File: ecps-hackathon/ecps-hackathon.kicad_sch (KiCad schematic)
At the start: 4 parts, among them U1 DHT11

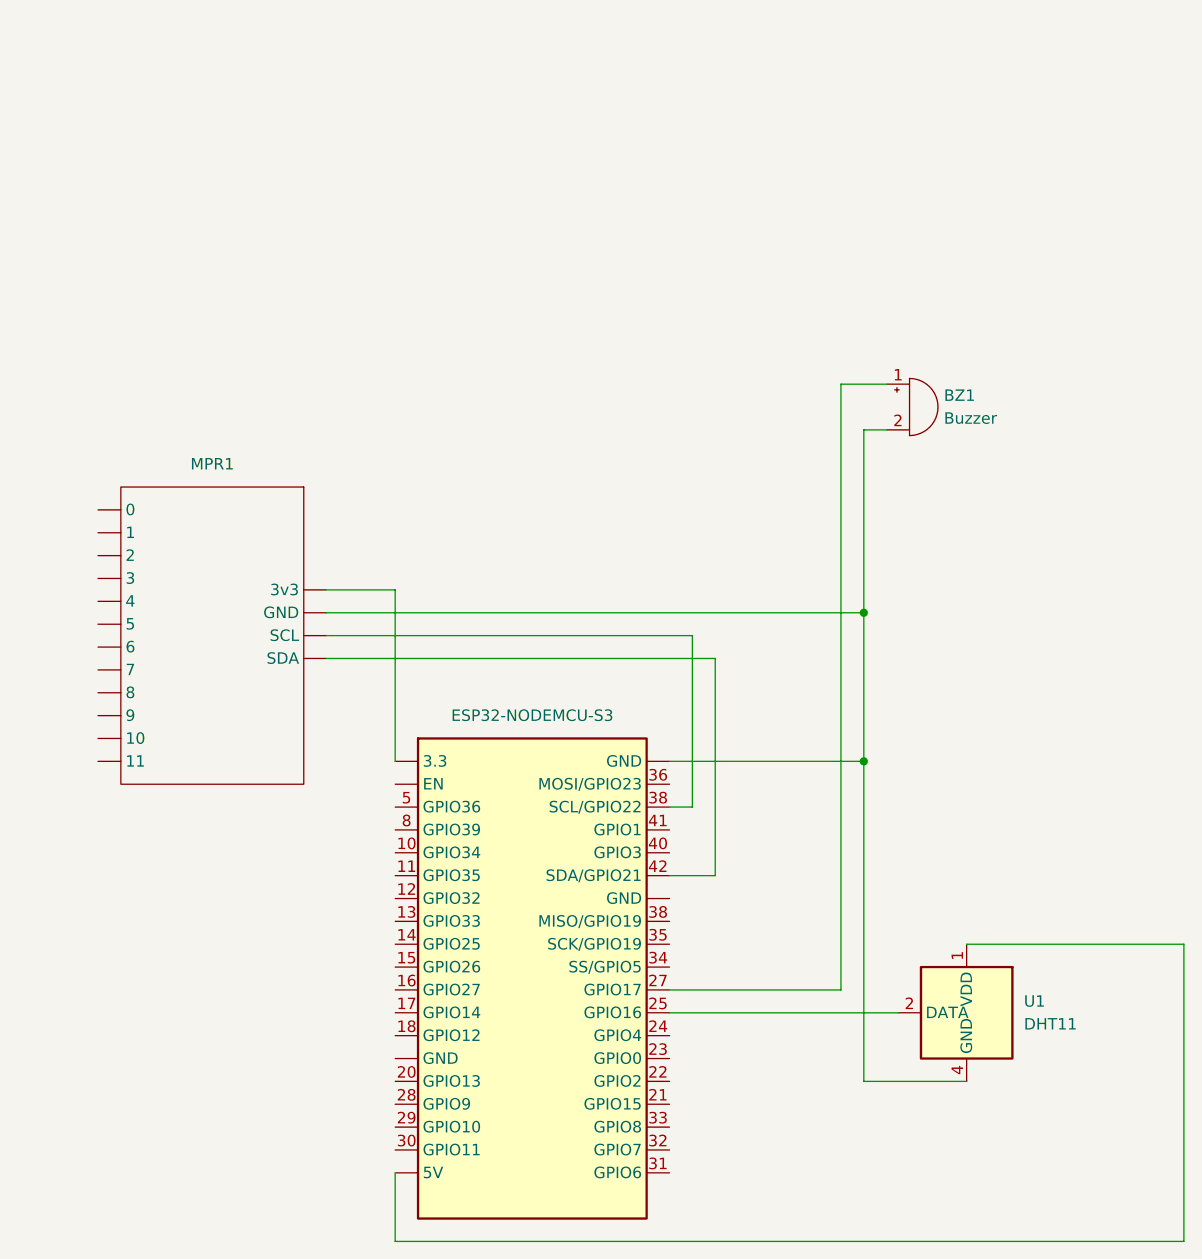
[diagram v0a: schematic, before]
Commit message: Update the kicad project to use rpi instead of esp
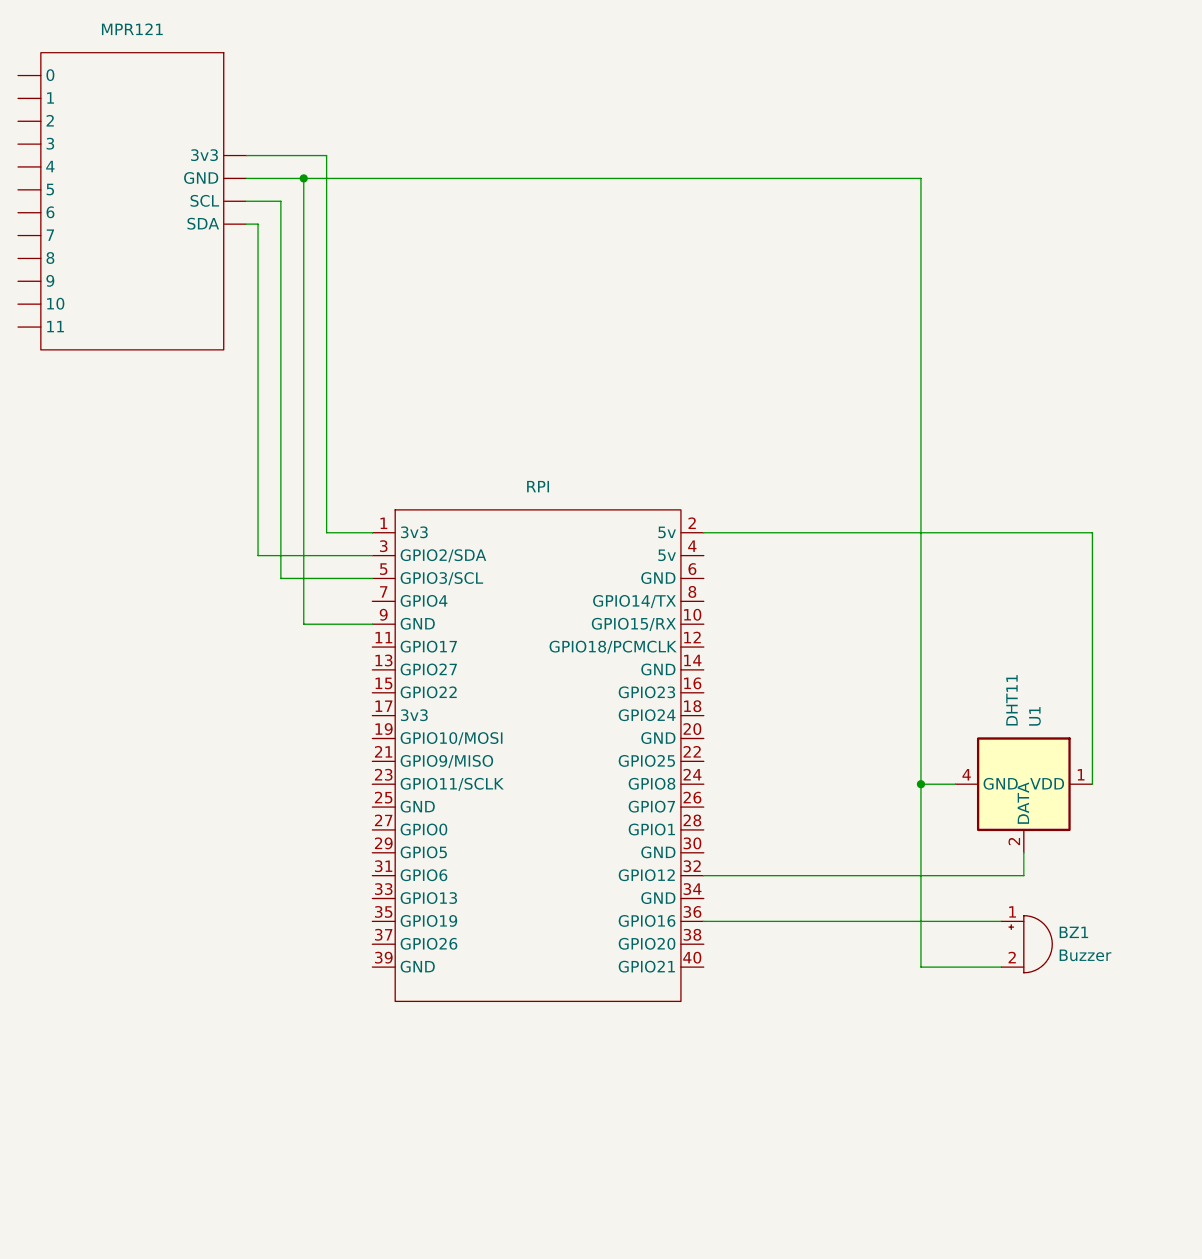
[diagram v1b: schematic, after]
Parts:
- removed 1: ESP32-NODEMCU-S3, symbol MECPS:ESP32-NODEMCU-S3
- added RPI: (no value), CM5IO:Raspberry-Pi-5-Compute-Module, symbol mecps:rpi_expansion
- renumbered MPR1 to MPR121
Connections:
- net at U1.1 (VDD): now also RPI.2 (5v)
- net at BZ1.2 (-), MPR121. (11), U1.4 (GND): now also RPI.9 (GND)
- net at U1.2 (DATA): now also RPI.32 (GPIO12)
- net at BZ1.1 (+): now also RPI.36 (GPIO16)
- new net: MPR121. (11), RPI.1 (3v3)
- new net: MPR121. (11), RPI.3 (GPIO2/SDA)
- new net: MPR121. (11), RPI.5 (GPIO3/SCL)
- now unconnected: MPR121. (11), MPR121. (11)
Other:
- moved on the sheet: BZ1, MPR121, U1
